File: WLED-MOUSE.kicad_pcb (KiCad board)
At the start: 2 copper layers, 1 part

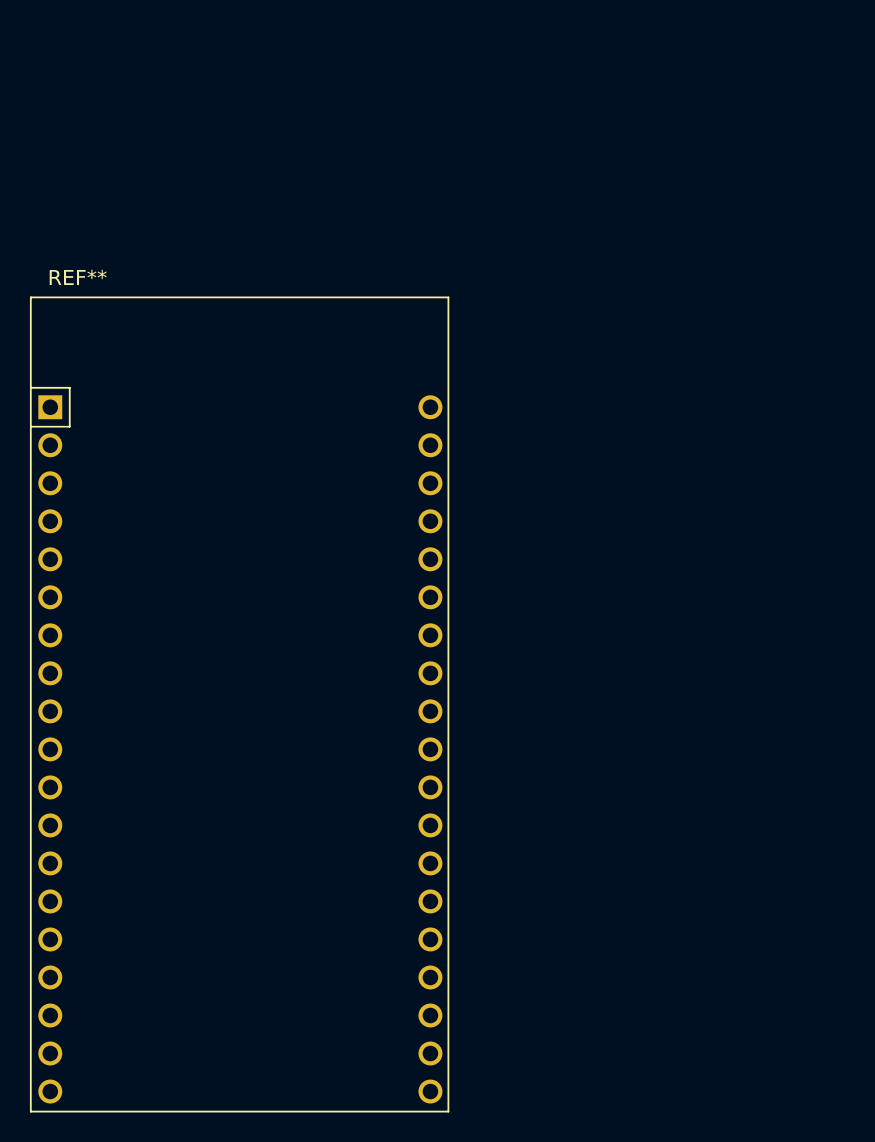
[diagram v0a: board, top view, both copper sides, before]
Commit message: added some footprints for components
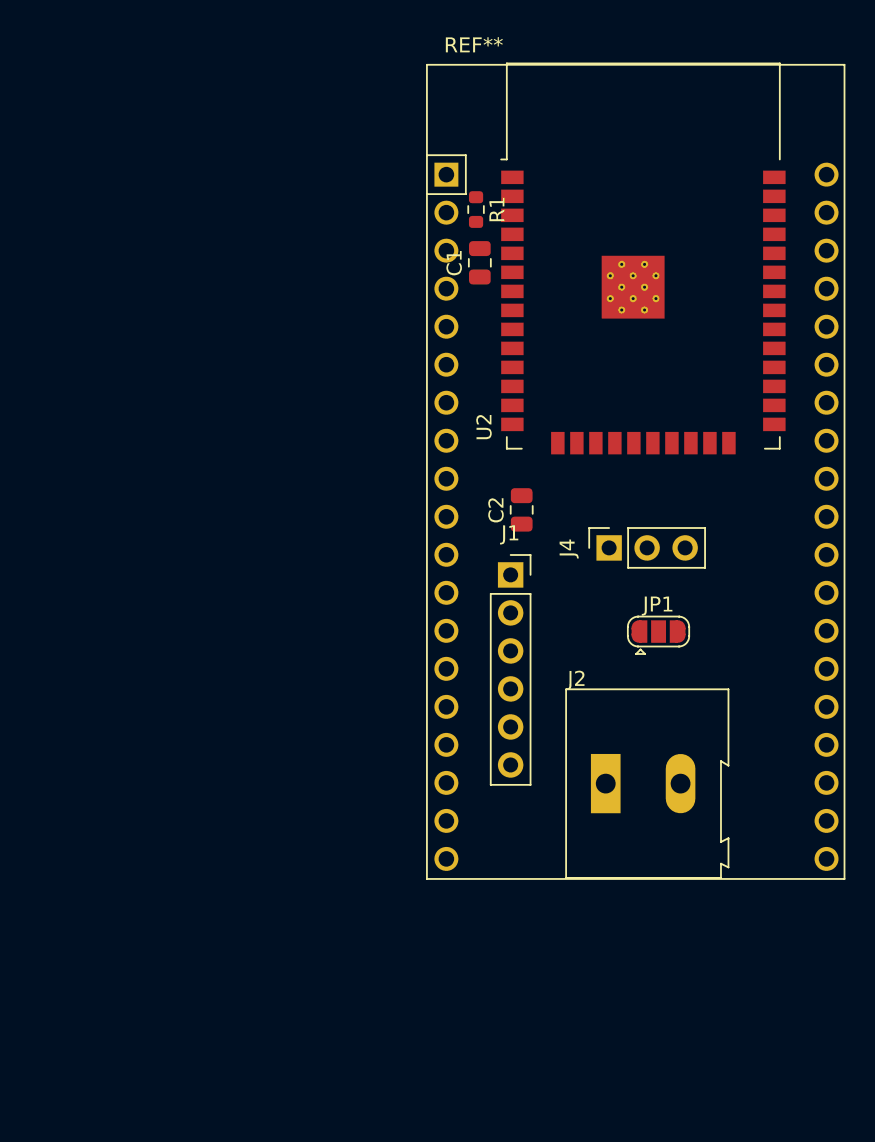
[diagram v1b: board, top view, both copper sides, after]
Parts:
- added C1: C, Capacitor_SMD:C_0805_2012Metric, F.Cu at (171.4, 86.9)
- added C2: 25uF, Capacitor_SMD:C_0805_2012Metric, F.Cu at (174.2, 103.4)
- added J1: FTDI-header, Connector_PinSocket_2.54mm:PinSocket_1x06_P2.54mm_Vertical, F.Cu at (173.5, 107.7)
- added J2: Power-in, TerminalBlock:TerminalBlock_Altech_AK300-2_P5.00mm, F.Cu at (179.9, 121.7)
- added J4: Pixel-strip, Connector_PinSocket_2.54mm:PinSocket_1x03_P2.54mm_Vertical, F.Cu at (180.1, 105.9)
- added JP1: SolderJumper_3_Bridged12, Jumper:SolderJumper-3_P1.3mm_Open_RoundedPad1.0x1.5mm, F.Cu at (183.4, 111.5)
- added R1: R, Resistor_SMD:R_0603_1608Metric, F.Cu at (171.2, 83.3)
- added U2: ESP32-WROOM-32D, RF_Module:ESP32-WROOM-32, F.Cu at (182.4, 89.4)
- moved REF** 30.7 mm to (169.2, 81.0)

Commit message: added some more nice little bits
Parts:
- added J6: Pixel-strip, Connector_PinSocket_2.54mm:PinSocket_1x03_P2.54mm_Vertical, F.Cu at (163.3, 111.3)
- added J7: Pixel-strip, Connector_PinSocket_2.54mm:PinSocket_1x03_P2.54mm_Vertical, F.Cu at (162.3, 99.3)
- added J8: Pixel-strip, Connector_PinSocket_2.54mm:PinSocket_1x03_P2.54mm_Vertical, F.Cu at (163.3, 86.4)
- added U3: SN74LV4T125, Package_SO:TSSOP-14_4.4x5mm_P0.65mm, F.Cu at (188.0, 105.2)
- moved J4 23.9 mm to (162.8, 122.4), turned to 0 degrees
- moved J2 15.0 mm to (179.9, 136.7)
